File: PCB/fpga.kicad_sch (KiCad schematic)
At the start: 18 parts, among them J8 Pin header, 2x4, J9 Pin header, 2x4, U4 LFE5U-25F-6BG256C, Y3 12MHz

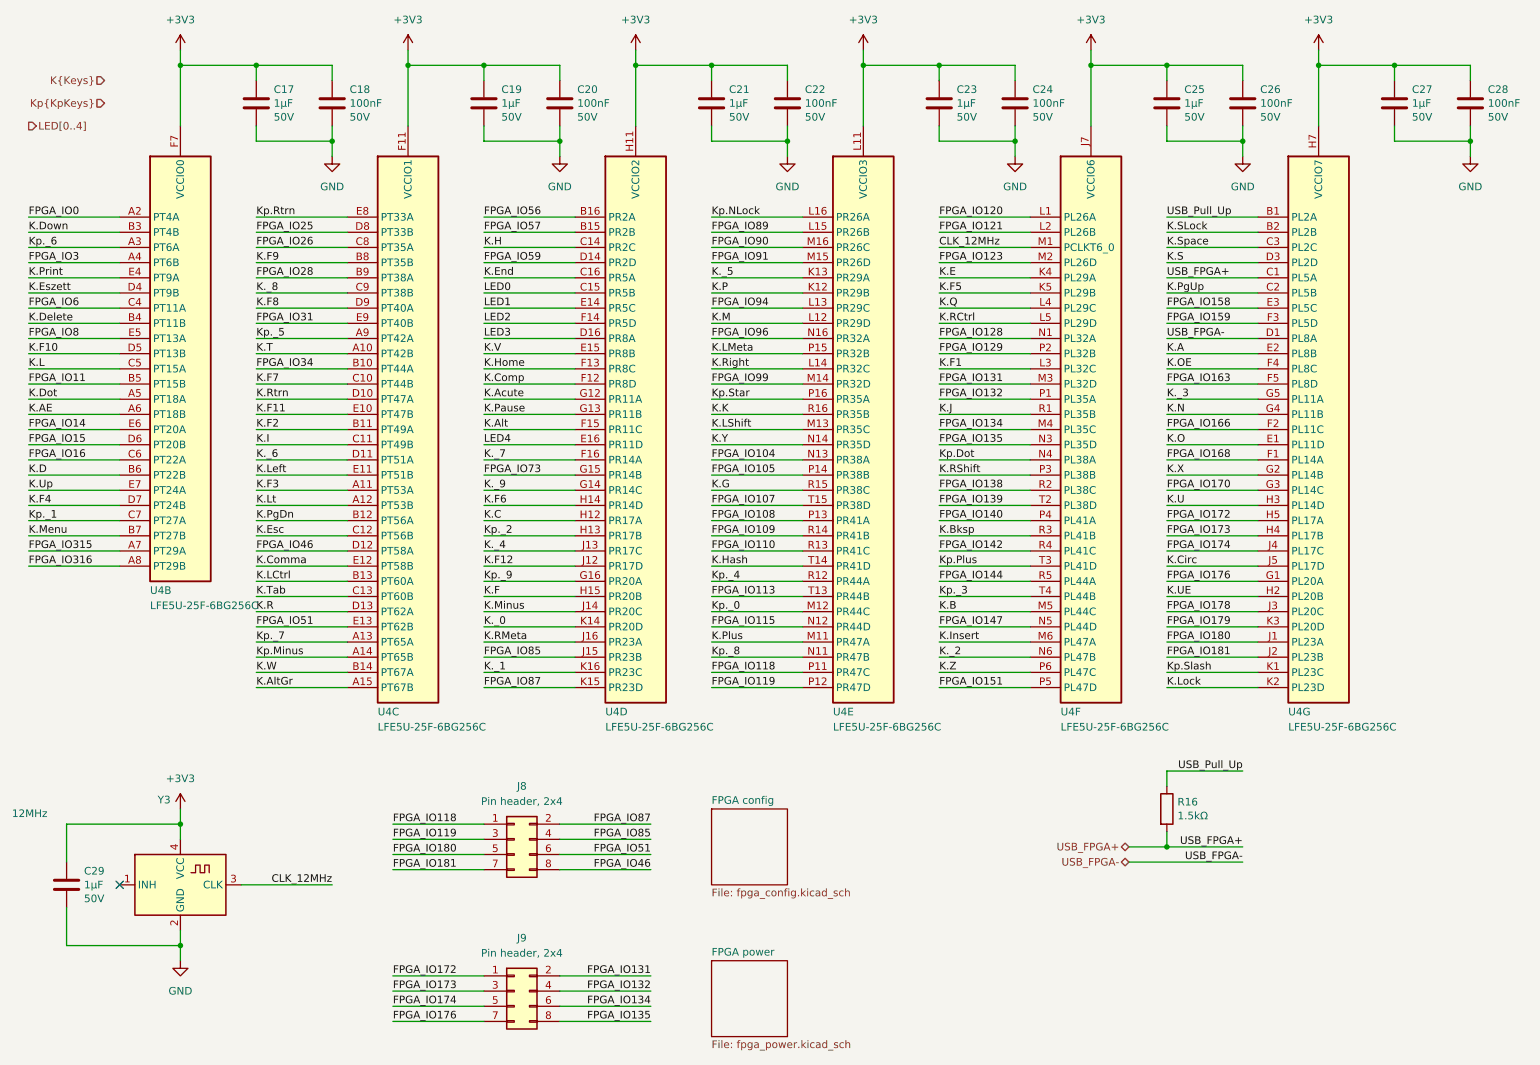
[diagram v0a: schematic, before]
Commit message: Fan-out the FPGA
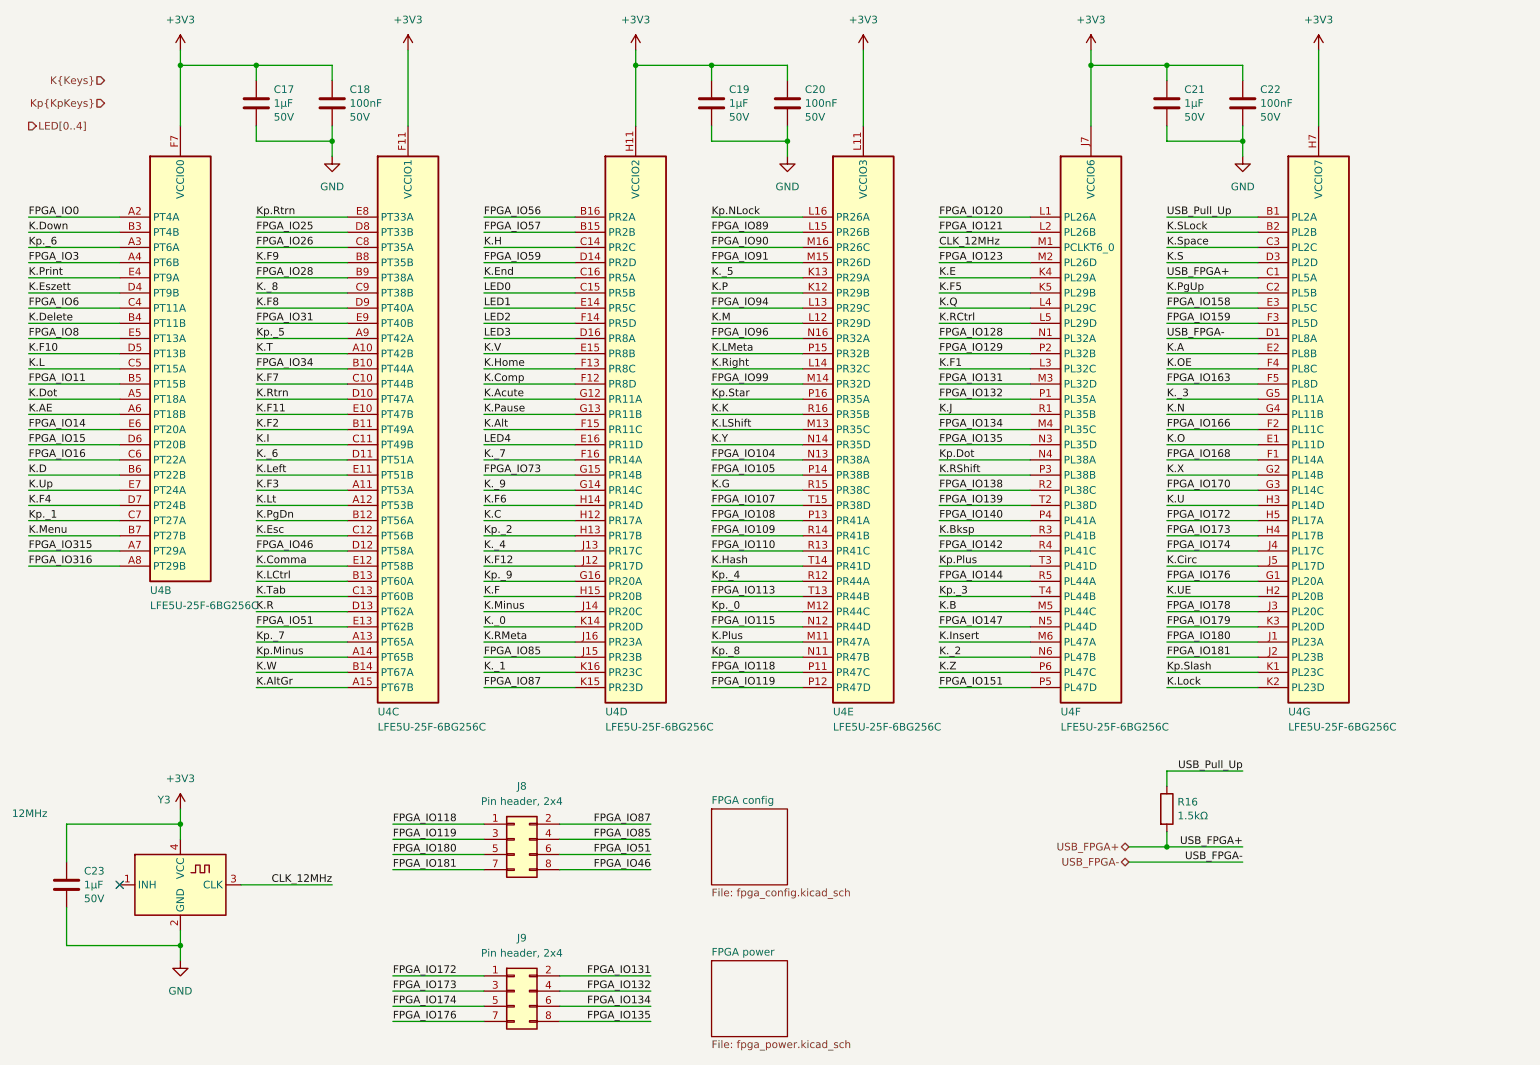
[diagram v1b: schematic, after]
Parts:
- removed C19, C23, C27: 1µF, Capacitor_SMD:C_0402_1005Metric_Pad0.74x0.62mm_HandSolder, symbol Device:C
- removed C20, C24, C28: 100nF, Capacitor_SMD:C_0402_1005Metric_Pad0.74x0.62mm_HandSolder, symbol Device:C
- renumbered C21 to C19, C22 to C20, C25 to C21, C26 to C22, C29 to C23

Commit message: Add ESD protection
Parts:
- removed J8, J9: Pin header, 2x4, Connector_PinHeader_2.54mm:PinHeader_2x04_P2.54mm_Vertical, symbol Connector_Generic:Conn_02x04_Odd_Even
- renumbered C17 to C26, C18 to C27, C19 to C28, C20 to C29, C21 to C30, C22 to C31, C23 to C32, R16 to R22, U4 to U13
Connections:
- net FPGA_IO118 renamed FPGA_GPIO0
- net FPGA_IO119 renamed FPGA_GPIO1
- net FPGA_IO131 renamed FPGA_GPIO12
- net FPGA_IO132 renamed FPGA_GPIO13
- net FPGA_IO134 renamed FPGA_GPIO14
- net FPGA_IO135 renamed FPGA_GPIO15
- net FPGA_IO172 renamed FPGA_GPIO8
- net FPGA_IO173 renamed FPGA_GPIO9
- net FPGA_IO174 renamed FPGA_GPIO10
- net FPGA_IO176 renamed FPGA_GPIO11
- net FPGA_IO180 renamed FPGA_GPIO2
- net FPGA_IO181 renamed FPGA_GPIO3
- net FPGA_IO46 renamed FPGA_GPIO7
- net FPGA_IO51 renamed FPGA_GPIO6
- net FPGA_IO85 renamed FPGA_GPIO5
- net FPGA_IO87 renamed FPGA_GPIO4
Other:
- added sheet FPGA GPIOs (fpga_gpio.kicad_sch)
- moved on the sheet: R22

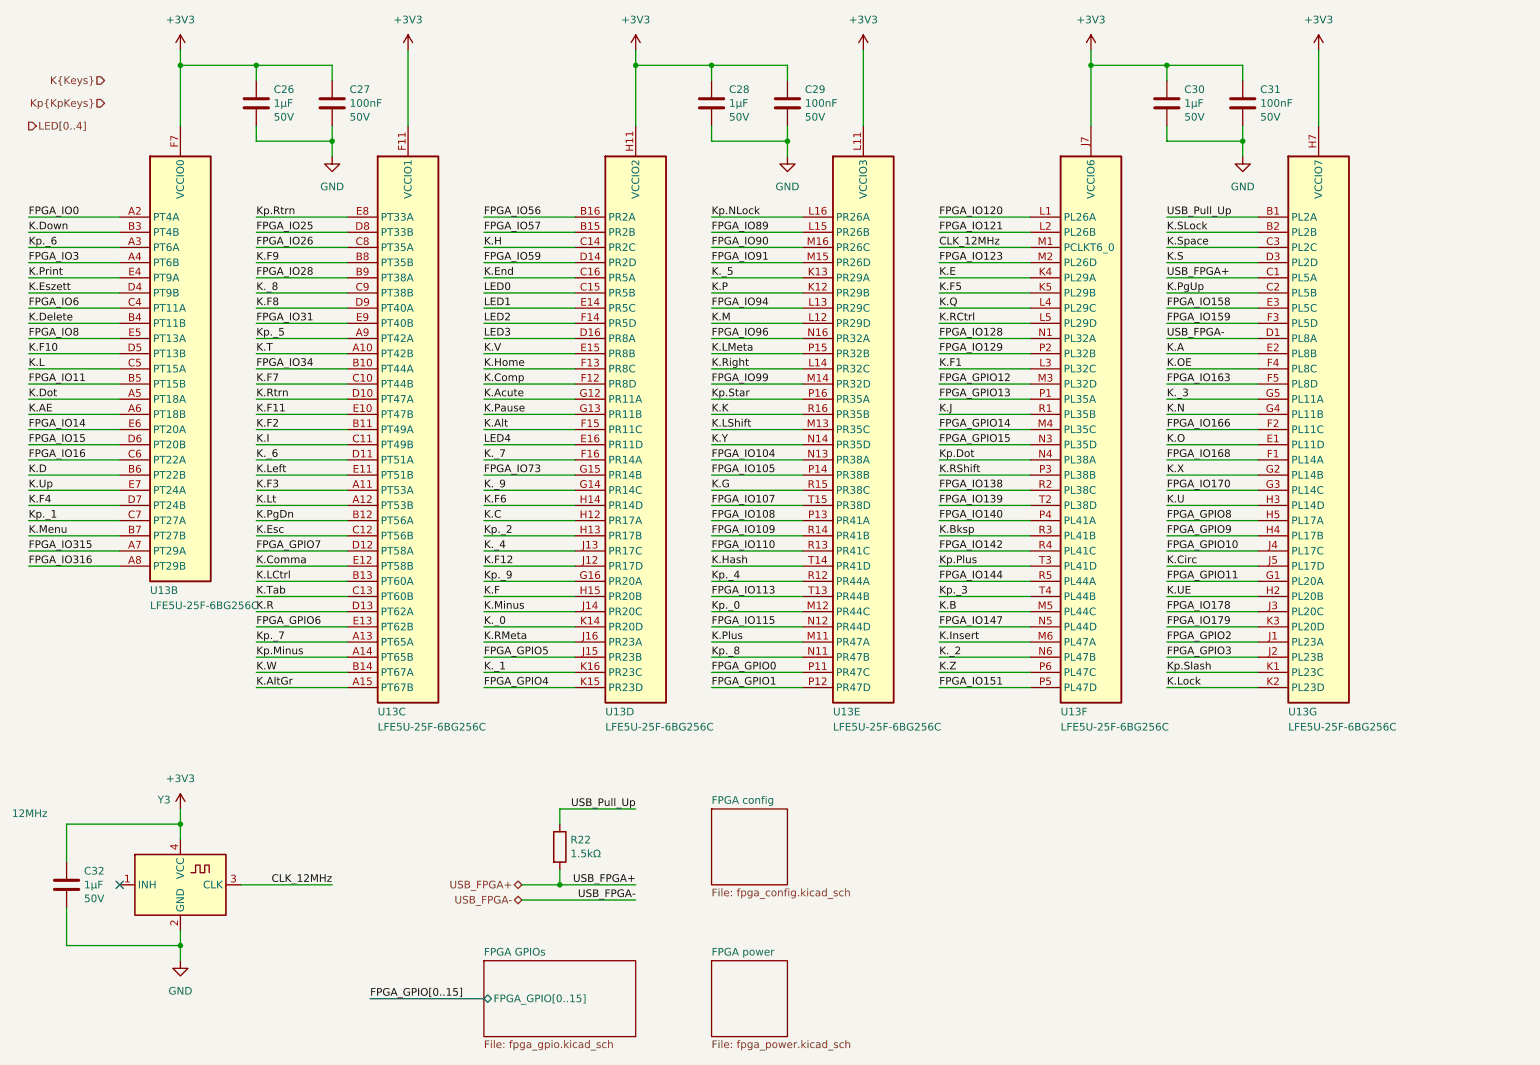
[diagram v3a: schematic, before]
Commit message: Complete the PCB routing
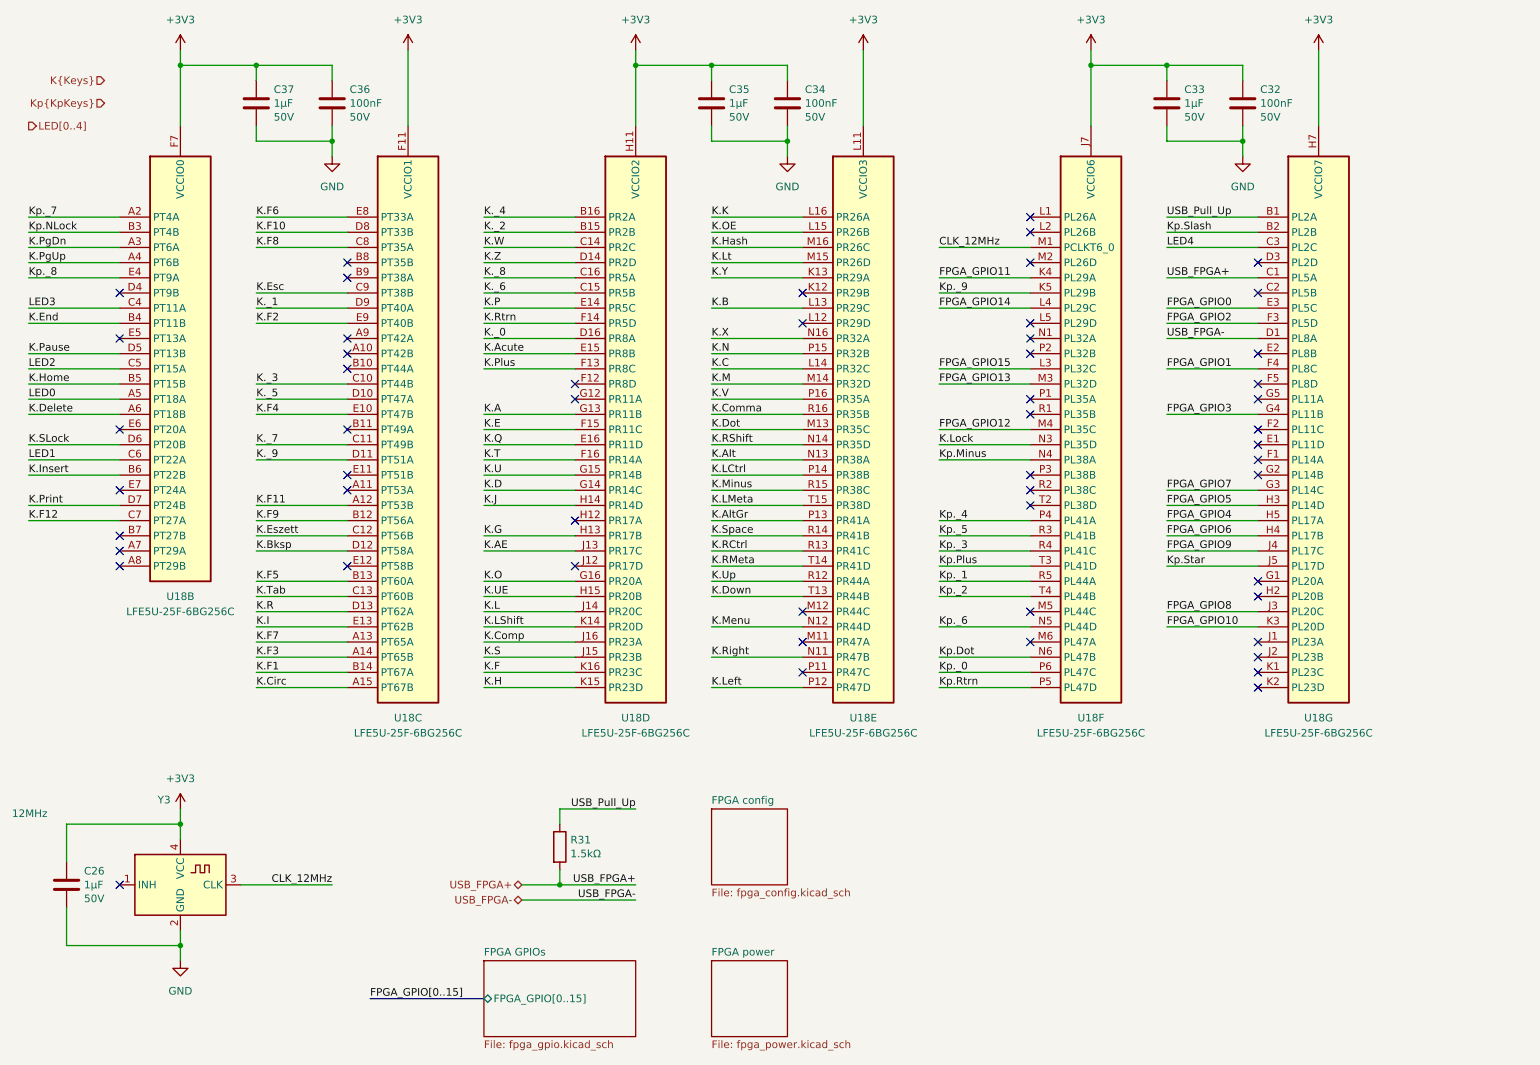
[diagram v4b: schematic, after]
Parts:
- renumbered C32 to C26, C31 to C32, C30 to C33, C29 to C34, C28 to C35, C27 to C36, C26 to C37, R22 to R31, U13 to U18
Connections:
- net FPGA_IO0 is gone; now on net Kp._7: U18.A2 (PT4A)
- net FPGA_IO104 is gone; now on net K.Alt: U18.N13 (PR38A)
- net FPGA_IO105 is gone; now on net K.LCtrl: U18.P14 (PR38B)
- net FPGA_IO107 is gone; now on net K.LMeta: U18.T15 (PR38D)
- net FPGA_IO108 is gone; now on net K.AltGr: U18.P13 (PR41A)
- net FPGA_IO109 is gone; now on net K.Space: U18.R14 (PR41B)
- net FPGA_IO11 is gone; now on net K.Home: U18.B5 (PT15B)
- net FPGA_IO110 is gone; now on net K.RCtrl: U18.R13 (PR41C)
- net FPGA_IO113 is gone; now on net K.Down: U18.T13 (PR44B)
- net FPGA_IO115 is gone; now on net K.Menu: U18.N12 (PR44D)
- net FPGA_IO140 is gone; now on net Kp._4: U18.P4 (PL41A)
- net FPGA_IO142 is gone; now on net Kp._3: U18.R4 (PL41C)
- net FPGA_IO144 is gone; now on net Kp._1: U18.R5 (PL44A)
- net FPGA_IO147 is gone; now on net Kp._6: U18.N5 (PL44D)
- net FPGA_IO15 is gone; now on net K.SLock: U18.D6 (PT20B)
- net FPGA_IO151 is gone; now on net Kp.Rtrn: U18.P5 (PL47D)
- net FPGA_IO158 is gone; now on net FPGA_GPIO0: U18.E3 (PL5C)
- net FPGA_IO159 is gone; now on net FPGA_GPIO2: U18.F3 (PL5D)
- net FPGA_IO16 is gone; now on net LED1: U18.C6 (PT22A)
- net FPGA_IO170 is gone; now on net FPGA_GPIO7: U18.G3 (PL14C)
- net FPGA_IO178 is gone; now on net FPGA_GPIO8: U18.J3 (PL20C)
- net FPGA_IO179 is gone; now on net FPGA_GPIO10: U18.K3 (PL20D)
- net FPGA_IO25 is gone; now on net K.F10: U18.D8 (PT33B)
- net FPGA_IO26 is gone; now on net K.F8: U18.C8 (PT35A)
- net FPGA_IO3 is gone; now on net K.PgUp: U18.A4 (PT6B)
- net FPGA_IO31 is gone; now on net K.F2: U18.E9 (PT40B)
- net FPGA_IO56 is gone; now on net K._4: U18.B16 (PR2A)
- net FPGA_IO57 is gone; now on net K._2: U18.B15 (PR2B)
- net FPGA_IO59 is gone; now on net K.Z: U18.D14 (PR2D)
- net FPGA_IO6 is gone; now on net LED3: U18.C4 (PT11A)
- net FPGA_IO73 is gone; now on net K.U: U18.G15 (PR14B)
- net FPGA_IO89 is gone; now on net K.OE: U18.L15 (PR26B)
- net FPGA_IO90 is gone; now on net K.Hash: U18.M16 (PR26C)
- net FPGA_IO91 is gone; now on net K.Lt: U18.M15 (PR26D)
- net FPGA_IO94 is gone; now on net K.B: U18.L13 (PR29C)
- net FPGA_IO96 is gone; now on net K.X: U18.N16 (PR32A)
- net FPGA_IO99 is gone; now on net K.M: U18.M14 (PR32D)
- net FPGA_GPIO0: no longer U18.P11 (PR47C)
- net FPGA_GPIO1: now also U18.F4 (PL8C); no longer U18.P12 (PR47D)
- net FPGA_GPIO10: no longer U18.J4 (PL17C)
- net FPGA_GPIO11: now also U18.K4 (PL29A); no longer U18.G1 (PL20A)
- net FPGA_GPIO12: now also U18.M4 (PL35C); no longer U18.M3 (PL32D)
- net FPGA_GPIO13: now also U18.M3 (PL32D); no longer U18.P1 (PL35A)
- net FPGA_GPIO14: now also U18.L4 (PL29C); no longer U18.M4 (PL35C)
- net FPGA_GPIO15: now also U18.L3 (PL32C); no longer U18.N3 (PL35D)
- net FPGA_GPIO2: no longer U18.J1 (PL23A)
- net FPGA_GPIO3: now also U18.G4 (PL11B); no longer U18.J2 (PL23B)
- net FPGA_GPIO4: now also U18.H5 (PL17A); no longer U18.K15 (PR23D)
- net FPGA_GPIO5: now also U18.H3 (PL14D); no longer U18.J15 (PR23B)
- net FPGA_GPIO6: now also U18.H4 (PL17B); no longer U18.E13 (PT62B)
- net FPGA_GPIO7: no longer U18.D12 (PT58A)
- net FPGA_GPIO8: no longer U18.H5 (PL17A)
- net FPGA_GPIO9: now also U18.J4 (PL17C); no longer U18.H4 (PL17B)
- net K.A: now also U18.G13 (PR11B); no longer U18.E2 (PL8B)
- net K.AE: now also U18.J13 (PR17C); no longer U18.A6 (PT18B)
- net K.Acute: now also U18.E15 (PR8B); no longer U18.G12 (PR11A)
- net K.Alt: no longer U18.F15 (PR11C)
- net K.AltGr: no longer U18.A15 (PT67B)
- net K.B: no longer U18.M5 (PL44C)
- net K.Bksp: now also U18.D12 (PT58A); no longer U18.R3 (PL41B)
- net K.C: now also U18.L14 (PR32C); no longer U18.H12 (PR17A)
- net K.Circ: now also U18.A15 (PT67B); no longer U18.J5 (PL17D)
- net K.Comma: now also U18.R16 (PR35B); no longer U18.E12 (PT58B)
- net K.Comp: now also U18.J16 (PR23A); no longer U18.F12 (PR8D)
- net K.D: now also U18.G14 (PR14C); no longer U18.B6 (PT22B)
- net K.Delete: now also U18.A6 (PT18B); no longer U18.B4 (PT11B)
- net K.Dot: now also U18.M13 (PR35C); no longer U18.A5 (PT18A)
- net K.Down: no longer U18.B3 (PT4B)
- net K.E: now also U18.F15 (PR11C); no longer U18.K4 (PL29A)
- net K.End: now also U18.B4 (PT11B); no longer U18.C16 (PR5A)
- net K.Esc: now also U18.C9 (PT38B); no longer U18.C12 (PT56B)
- net K.Eszett: now also U18.C12 (PT56B); no longer U18.D4 (PT9B)
- net K.F: now also U18.K16 (PR23C); no longer U18.H15 (PR20B)
- net K.F1: now also U18.B14 (PT67A); no longer U18.L3 (PL32C)
- net K.F10: no longer U18.D5 (PT13B)
- net K.F11: now also U18.A12 (PT53B); no longer U18.E10 (PT47B)
- net K.F12: now also U18.C7 (PT27A); no longer U18.J12 (PR17D)
- net K.F2: no longer U18.B11 (PT49A)
- net K.F3: now also U18.A14 (PT65B); no longer U18.A11 (PT53A)
- net K.F4: now also U18.E10 (PT47B); no longer U18.D7 (PT24B)
- net K.F5: now also U18.B13 (PT60A); no longer U18.K5 (PL29B)
- net K.F6: now also U18.E8 (PT33A); no longer U18.H14 (PR14D)
- net K.F7: now also U18.A13 (PT65A); no longer U18.C10 (PT44B)
- net K.F8: no longer U18.D9 (PT40A)
- net K.F9: now also U18.B12 (PT56A); no longer U18.B8 (PT35B)
- net K.G: now also U18.H13 (PR17B); no longer U18.R15 (PR38C)
- net K.H: now also U18.K15 (PR23D); no longer U18.C14 (PR2C)
- net K.Hash: no longer U18.T14 (PR41D)
- net K.Home: no longer U18.F13 (PR8C)
- net K.I: now also U18.E13 (PT62B); no longer U18.C11 (PT49B)
- net K.Insert: now also U18.B6 (PT22B); no longer U18.M6 (PL47A)
- net K.J: now also U18.H14 (PR14D); no longer U18.R1 (PL35B)
- net K.K: now also U18.L16 (PR26A); no longer U18.R16 (PR35B)
- net K.L: now also U18.J14 (PR20C); no longer U18.C5 (PT15A)
- net K.LCtrl: no longer U18.B13 (PT60A)
- net K.LMeta: no longer U18.P15 (PR32B)
- net K.LShift: now also U18.K14 (PR20D); no longer U18.M13 (PR35C)
- net K.Left: now also U18.P12 (PR47D); no longer U18.E11 (PT51B)
- net K.Lock: now also U18.N3 (PL35D); no longer U18.K2 (PL23D)
- net K.Lt: no longer U18.A12 (PT53B)
- net K.M: no longer U18.L12 (PR29D)
- net K.Menu: no longer U18.B7 (PT27B)
- net K.Minus: now also U18.R15 (PR38C); no longer U18.J14 (PR20C)
- net K.N: now also U18.P15 (PR32B); no longer U18.G4 (PL11B)
- net K.O: now also U18.G16 (PR20A); no longer U18.E1 (PL11D)
- net K.OE: no longer U18.F4 (PL8C)
- net K.P: now also U18.E14 (PR5C); no longer U18.K12 (PR29B)
- net K.Pause: now also U18.D5 (PT13B); no longer U18.G13 (PR11B)
- net K.PgDn: now also U18.A3 (PT6A); no longer U18.B12 (PT56A)
- net K.PgUp: no longer U18.C2 (PL5B)
- net K.Plus: now also U18.F13 (PR8C); no longer U18.M11 (PR47A)
- net K.Print: now also U18.D7 (PT24B); no longer U18.E4 (PT9A)
- net K.Q: now also U18.E16 (PR11D); no longer U18.L4 (PL29C)
- net K.RCtrl: no longer U18.L5 (PL29D)
- net K.RMeta: now also U18.T14 (PR41D); no longer U18.J16 (PR23A)
- net K.RShift: now also U18.N14 (PR35D); no longer U18.P3 (PL38B)
- net K.Right: now also U18.N11 (PR47B); no longer U18.L14 (PR32C)
- net K.Rtrn: now also U18.F14 (PR5D); no longer U18.D10 (PT47A)
- net K.S: now also U18.J15 (PR23B); no longer U18.D3 (PL2D)
- net K.SLock: no longer U18.B2 (PL2B)
- net K.Space: no longer U18.C3 (PL2C)
- net K.T: now also U18.F16 (PR14A); no longer U18.A10 (PT42B)
- net K.U: no longer U18.H3 (PL14D)
- net K.UE: now also U18.H15 (PR20B); no longer U18.H2 (PL20B)
- net K.Up: now also U18.R12 (PR44A); no longer U18.E7 (PT24A)
- net K.V: now also U18.P16 (PR35A); no longer U18.E15 (PR8B)
- net K.W: now also U18.C14 (PR2C); no longer U18.B14 (PT67A)
- net K.X: no longer U18.G2 (PL14B)
- net K.Y: now also U18.K13 (PR29A); no longer U18.N14 (PR35D)
- net K.Z: no longer U18.P6 (PL47C)
- net K._0: now also U18.D16 (PR8A); no longer U18.K14 (PR20D)
- net K._1: now also U18.D9 (PT40A); no longer U18.K16 (PR23C)
- net K._2: no longer U18.N6 (PL47B)
- net K._3: now also U18.C10 (PT44B); no longer U18.G5 (PL11A)
- net K._4: no longer U18.J13 (PR17C)
- net K._5: now also U18.D10 (PT47A); no longer U18.K13 (PR29A)
- net K._6: now also U18.C15 (PR5B); no longer U18.D11 (PT51A)
- net K._7: now also U18.C11 (PT49B); no longer U18.F16 (PR14A)
- net K._8: now also U18.C16 (PR5A); no longer U18.C9 (PT38B)
- net K._9: now also U18.D11 (PT51A); no longer U18.G14 (PR14C)
- net Kp.Dot: now also U18.N6 (PL47B); no longer U18.N4 (PL38A)
- net Kp.Minus: now also U18.N4 (PL38A); no longer U18.A14 (PT65B)
- net Kp.NLock: now also U18.B3 (PT4B); no longer U18.L16 (PR26A)
- net Kp.Rtrn: no longer U18.E8 (PT33A)
- net Kp.Slash: now also U18.B2 (PL2B); no longer U18.K1 (PL23C)
- net Kp.Star: now also U18.J5 (PL17D); no longer U18.P16 (PR35A)
- net Kp._0: now also U18.P6 (PL47C); no longer U18.M12 (PR44C)
- net Kp._1: no longer U18.C7 (PT27A)
- net Kp._2: now also U18.T4 (PL44B); no longer U18.H13 (PR17B)
- net Kp._3: no longer U18.T4 (PL44B)
- net Kp._4: no longer U18.R12 (PR44A)
- net Kp._5: now also U18.R3 (PL41B); no longer U18.A9 (PT42A)
- net Kp._6: no longer U18.A3 (PT6A)
- net Kp._7: no longer U18.A13 (PT65A)
- net Kp._8: now also U18.E4 (PT9A); no longer U18.N11 (PR47B)
- net Kp._9: now also U18.K5 (PL29B); no longer U18.G16 (PR20A)
- net LED0: now also U18.A5 (PT18A); no longer U18.C15 (PR5B)
- net LED1: no longer U18.E14 (PR5C)
- net LED2: now also U18.C5 (PT15A); no longer U18.F14 (PR5D)
- net LED3: no longer U18.D16 (PR8A)
- net LED4: now also U18.C3 (PL2C); no longer U18.E16 (PR11D)
- net FPGA_IO120: no longer names the net of U18.L1 (PL26A)
- net FPGA_IO121: no longer names the net of U18.L2 (PL26B)
- net FPGA_IO123: no longer names the net of U18.M2 (PL26D)
- net FPGA_IO128: no longer names the net of U18.N1 (PL32A)
- net FPGA_IO129: no longer names the net of U18.P2 (PL32B)
- net FPGA_IO138: no longer names the net of U18.R2 (PL38C)
- net FPGA_IO139: no longer names the net of U18.T2 (PL38D)
- net FPGA_IO14: no longer names the net of U18.E6 (PT20A)
- net FPGA_IO163: no longer names the net of U18.F5 (PL8D)
- net FPGA_IO166: no longer names the net of U18.F2 (PL11C)
- net FPGA_IO168: no longer names the net of U18.F1 (PL14A)
- net FPGA_IO28: no longer names the net of U18.B9 (PT38A)
- net FPGA_IO315: no longer names the net of U18.A7 (PT29A)
- net FPGA_IO316: no longer names the net of U18.A8 (PT29B)
- net FPGA_IO34: no longer names the net of U18.B10 (PT44A)
- net FPGA_IO8: no longer names the net of U18.E5 (PT13A)
- no-connect marks 1 -> 54
